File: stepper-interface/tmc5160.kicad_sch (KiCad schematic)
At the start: 30 parts, among them J401 Molex_Pico-SPOX_Horizontal, J402 Molex_Pico-SPOX_Horizontal, U401 TMC5160A-WA, U402 MAX6816, X401 16MHz

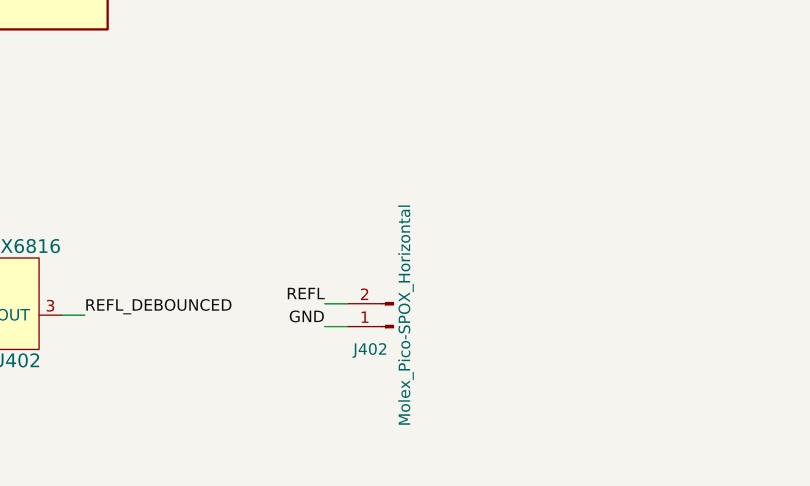
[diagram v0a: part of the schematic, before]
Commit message: Update fan controls
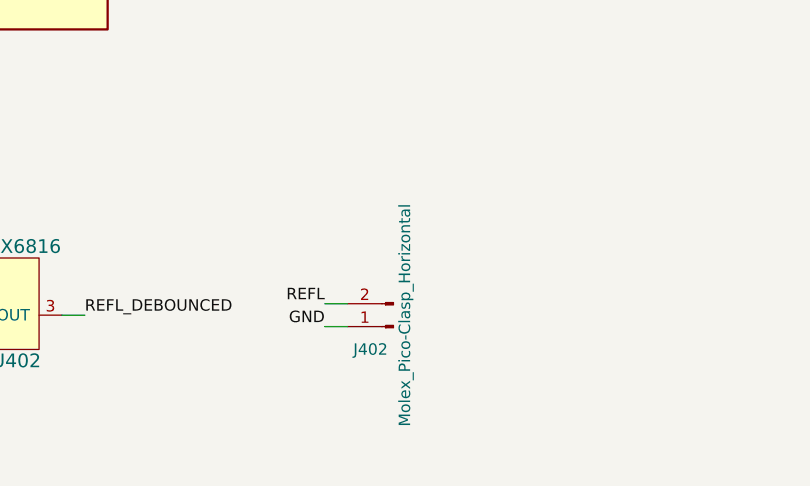
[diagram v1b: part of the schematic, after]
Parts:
- J402: value Molex_Pico-SPOX_Horizontal -> Molex_Pico-Clasp_Horizontal
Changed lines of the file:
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@@
   (title_block
     (title "stepper-interface")
-    (date "2024-04-29")
+    (date "2024-04-30")
     (rev "1.0")
     (company "Howard Hughes Medical Institute")
@@
     )
   )
+  (symbol (lib_id "Janelia:Conn_01x02_P1mm_Molex_Pico-Clasp-501330_Horizontal") (at 101.6 177.8 180) (unit 1)
+    (in_bom yes) (on_board yes) (dnp no) (fields_autoplaced)
+    (property "Reference" "J402" (at 99.06 180.34 0) (do_not_autoplace)
+      (effects (font (size 1.27 1.27)))
+    )
+    (property "Value" "Molex_Pico-Clasp_Horizontal" (at 102.87 176.53 90) (do_not_autoplace)
+      (effects (font (size 1.27 1.27)))
+    )
+    (property "Footprint" "Janelia:Molex_Pico-Clasp-501568_1x02_P1mm_Horizontal" (at 101.6 177.8 0)
+      (effects (font (size 1.27 1.27)) hide)
+    )
+    (property "Datasheet" "~" (at 101.6 177.8 0)
+      (effects (font (size 1.27 1.27)) hide)
+    )
+    (property "Synopsis" "CONN HEADER SMD R/A 2POS 1MM" (at 101.6 177.8 0)
+      (effects (font (size 1.27 1.27)) hide)
+    )
+    (property "Manufacturer" "Molex" (at 101.6 177.8 0)
+      (effects (font (size 1.27 1.27)) hide)
+    )
+    (property "Manufactuer Part Number" "5015680207" (at 101.6 177.8 0)
+      (effects (font (size 1.27 1.27)) hide)
+    )
+    (property "Vendor" "Digi-Key" (at 101.6 177.8 0)
+      (effects (font (size 1.27 1.27)) hide)
+    )
+    (property "Vendor Part Number" "WM7893CT-ND" (at 101.6 177.8 0)
+      (effects (font (size 1.27 1.27)) hide)
+    )
+    (pin "2")
+    (pin "1")
+    (instances
+      (project "stepper-interface"
+        (path "/df2b2e89-e055-4140-95de-f1df723db034/039ac378-5273-4081-85bf-9eb26cb5ed57"
+          (reference "J402") (unit 1)
+        )
+      )
+    )
+  )
   (symbol (lib_id "Janelia:R_47_0.063W_0402") (at 128.27 111.76 90) (unit 1)
     (in_bom yes) (on_board yes) (dnp no)
@@
         )
       )
-    )
-  )
-  (symbol (lib_id "Janelia:Conn_01x02_P1mm_Molex_Pico-Clasp-501330_Horizontal") (at 101.6 177.8 180) (unit 1)
-    (in_bom yes) (on_board yes) (dnp no)
-    (property "Reference" "J402" (at 99.06 180.34 0) (do_not_autoplace)
-      (effects (font (size 1.27 1.27)))
-    )
-    (property "Value" "Molex_Pico-SPOX_Horizontal" (at 102.87 176.53 90) (do_not_autoplace)
-      (effects (font (size 1.27 1.27)))
-    )
-    (property "Footprint" "Janelia:Molex_Pico-Clasp-501568_1x02_P1mm_Horizontal" (at 101.6 177.8 0)
-      (effects (font (size 1.27 1.27)) hide)
-    )
-    (property "Datasheet" "~" (at 101.6 177.8 0)
-      (effects (font (size 1.27 1.27)) hide)
-    )
-    (property "Manufacturer" "Molex" (at 101.6 177.8 0)
-      (effects (font (size 1.27 1.27)) hide)
-    )
-    (property "Manufactuer Part Number" "5015680207" (at 101.6 177.8 0)
-      (effects (font (size 1.27 1.27)) hide)
-    )
-    (property "Vendor" "Digi-Key" (at 101.6 177.8 0)
-      (effects (font (size 1.27 1.27)) hide)
-    )
-    (property "Vendor Part Number" "WM7893CT-ND" (at 101.6 177.8 0)
-      (effects (font (size 1.27 1.27)) hide)
-    )
-    (property "Synopsis" "CONN HEADER SMD R/A 2POS 1MM" (at 101.6 177.8 0)
-      (effects (font (size 1.27 1.27)) hide)
-    )
-    (pin "1")
-    (pin "2")
-    (instances
-      (project "stepper-interface"
-        (path "/df2b2e89-e055-4140-95de-f1df723db034/039ac378-5273-4081-85bf-9eb26cb5ed57"
-          (reference "J402") (unit 1)
-        )
-      )

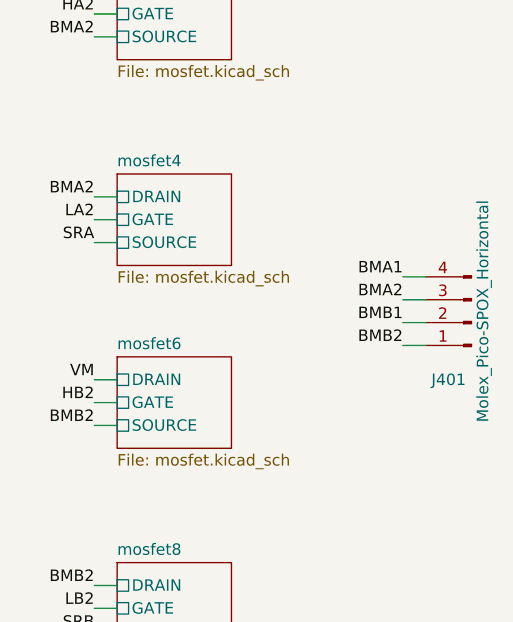
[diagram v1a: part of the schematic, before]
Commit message: Fix warnings on import from schematic to pcb
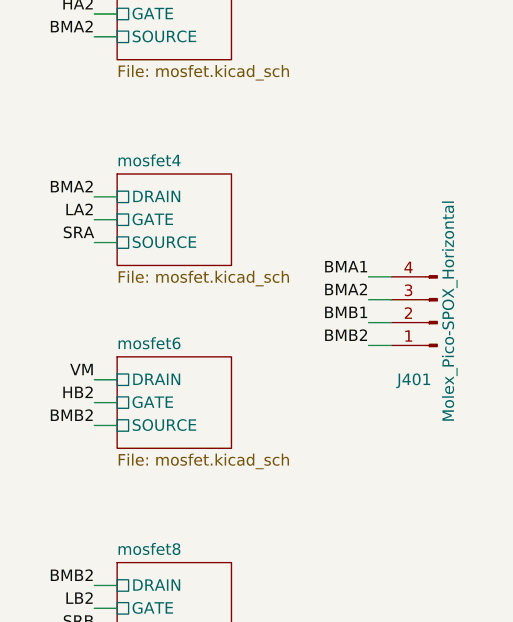
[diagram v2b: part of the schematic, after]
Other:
- moved on the sheet: J401
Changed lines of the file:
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@@
   (title_block
     (title "stepper-interface")
-    (date "2024-04-30")
+    (date "2024-05-01")
     (rev "1.0")
     (company "Howard Hughes Medical Institute")
@@
     (stroke (width 0) (type default))
   )
-  (wire (pts (xy 273.05 123.19) (xy 275.59 123.19))
+  (wire (pts (xy 269.24 123.19) (xy 271.78 123.19))
     (stroke (width 0) (type default))
   )
@@
     (stroke (width 0) (type default))
   )
-  (wire (pts (xy 273.05 120.65) (xy 275.59 120.65))
+  (wire (pts (xy 269.24 120.65) (xy 271.78 120.65))
     (stroke (width 0) (type default))
   )
@@
     (stroke (width 0) (type default))
   )
-  (wire (pts (xy 273.05 128.27) (xy 275.59 128.27))
+  (wire (pts (xy 269.24 128.27) (xy 271.78 128.27))
     (stroke (width 0) (type default))
   )
@@
     (stroke (width 0) (type default))
   )
-  (wire (pts (xy 273.05 125.73) (xy 275.59 125.73))
+  (wire (pts (xy 269.24 125.73) (xy 271.78 125.73))
     (stroke (width 0) (type default))
   )
@@
     (effects (font (size 1.27 1.27)) (justify left bottom))
   )
-  (label "BMA1" (at 273.05 120.65 180) (fields_autoplaced)
+  (label "BMA1" (at 269.24 120.65 180) (fields_autoplaced)
     (effects (font (size 1.27 1.27)) (justify right bottom))
   )
@@
     (effects (font (size 1.27 1.27)) (justify left bottom))
   )
-  (label "BMA2" (at 273.05 123.19 180) (fields_autoplaced)
+  (label "BMA2" (at 269.24 123.19 180) (fields_autoplaced)
     (effects (font (size 1.27 1.27)) (justify right bottom))
   )
@@
     (effects (font (size 1.27 1.27)) (justify right bottom))
   )
-  (label "BMB1" (at 273.05 125.73 180) (fields_autoplaced)
+  (label "BMB1" (at 269.24 125.73 180) (fields_autoplaced)
     (effects (font (size 1.27 1.27)) (justify right bottom))
   )
@@
     (effects (font (size 1.27 1.27)) (justify right bottom))
   )
-  (label "BMB2" (at 273.05 128.27 180) (fields_autoplaced)
+  (label "BMB2" (at 269.24 128.27 180) (fields_autoplaced)
     (effects (font (size 1.27 1.27)) (justify right bottom))
   )
@@
     )
   )
-  (symbol (lib_id "Janelia:Conn_01x04_P1.5mm_Molex_Pico-SPOX-87438_Horizontal") (at 280.67 125.73 180) (unit 1)
+  (symbol (lib_id "Janelia:Conn_01x04_P1.5mm_Molex_Pico-SPOX-87438_Horizontal") (at 276.86 125.73 180) (unit 1)
     (in_bom yes) (on_board yes) (dnp no)
-    (property "Reference" "J401" (at 278.13 132.08 0) (do_not_autoplace)
+    (property "Reference" "J401" (at 274.32 132.08 0) (do_not_autoplace)
       (effects (font (size 1.27 1.27)))
     )
-    (property "Value" "Molex_Pico-SPOX_Horizontal" (at 281.94 124.46 90) (do_not_autoplace)
+    (property "Value" "Molex_Pico-SPOX_Horizontal" (at 278.13 124.46 90) (do_not_autoplace)
       (effects (font (size 1.27 1.27)))
     )
-    (property "Footprint" "Janelia:Molex_Pico-SPOX-87438_1x04-P1.5mm_Horizontal" (at 280.67 125.73 0)
-      (effects (font (size 1.27 1.27)) hide)
-    )
-    (property "Datasheet" "~" (at 280.67 125.73 0)
-      (effects (font (size 1.27 1.27)) hide)
-    )
-    (property "Manufacturer" "Molex" (at 280.67 125.73 0)
-      (effects (font (size 1.27 1.27)) hide)
-    )
-    (property "Manufacturer Part Number" "0874380443" (at 280.67 125.73 0)
-      (effects (font (size 1.27 1.27)) hide)
-    )
-    (property "Vendor" "Digi-Key" (at 280.67 125.73 0)
-      (effects (font (size 1.27 1.27)) hide)
-    )
-    (property "Vendor Part Number" "WM7648CT-ND" (at 280.67 125.73 0)
-      (effects (font (size 1.27 1.27)) hide)
-    )
-    (property "Synopsis" "CONN HEADER SMD R/A 4POS 1.5MM" (at 280.67 125.73 0)
+    (property "Footprint" "Janelia:Molex_Pico-SPOX-87438_1x04-P1.5mm_Horizontal" (at 276.86 125.73 0)
+      (effects (font (size 1.27 1.27)) hide)
+    )
+    (property "Datasheet" "~" (at 276.86 125.73 0)
+      (effects (font (size 1.27 1.27)) hide)
+    )
+    (property "Manufacturer" "Molex" (at 276.86 125.73 0)
+      (effects (font (size 1.27 1.27)) hide)
+    )
+    (property "Manufacturer Part Number" "0874380443" (at 276.86 125.73 0)
+      (effects (font (size 1.27 1.27)) hide)
+    )
+    (property "Vendor" "Digi-Key" (at 276.86 125.73 0)
+      (effects (font (size 1.27 1.27)) hide)
+    )
+    (property "Vendor Part Number" "WM7648CT-ND" (at 276.86 125.73 0)
+      (effects (font (size 1.27 1.27)) hide)
+    )
+    (property "Synopsis" "CONN HEADER SMD R/A 4POS 1.5MM" (at 276.86 125.73 0)
       (effects (font (size 1.27 1.27)) hide)
     )
@@
     (pin "2")
     (pin "1")
-    (instances
-      (project "stepper-interface"
+    (pin "MP")
+    (instances
+      (project "stepper-interface"
